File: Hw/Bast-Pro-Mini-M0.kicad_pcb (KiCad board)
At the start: 2 copper layers, 17.8 x 33 mm, 24 parts, among them J1 USB_B_Micro, J2 Conn_02x02_Odd_Even, P1 Digital, P2 ADC, P3 Analog, U1 AP2112K-3.3TRG1, U2 ATSAMD21E18A-AF

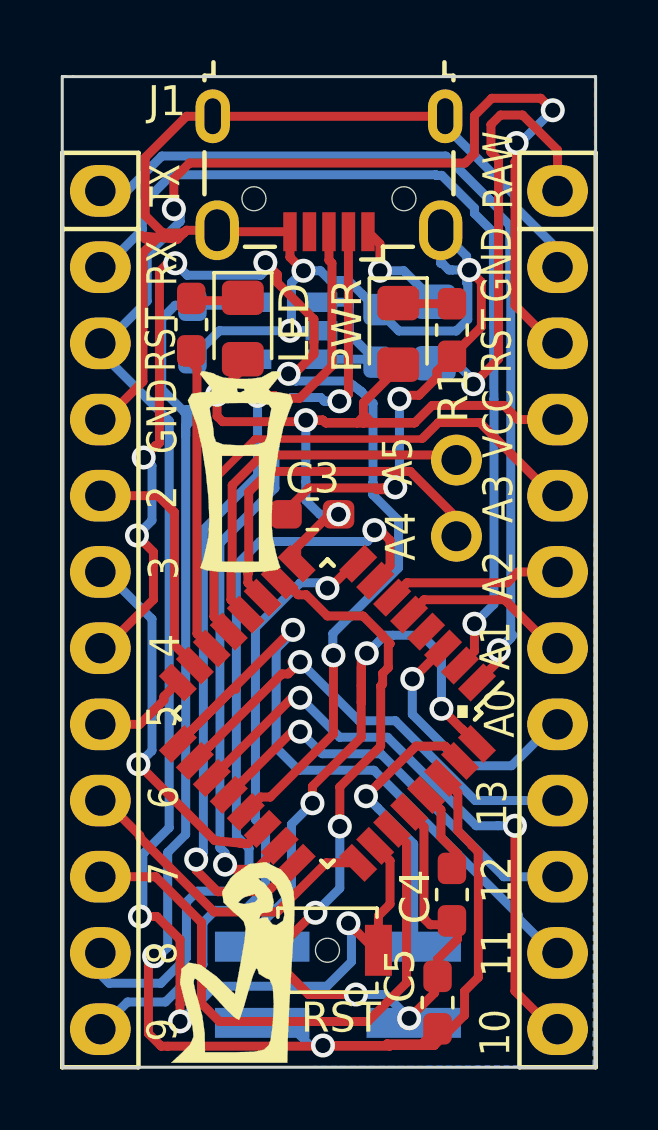
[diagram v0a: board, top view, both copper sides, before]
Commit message: Change type of button
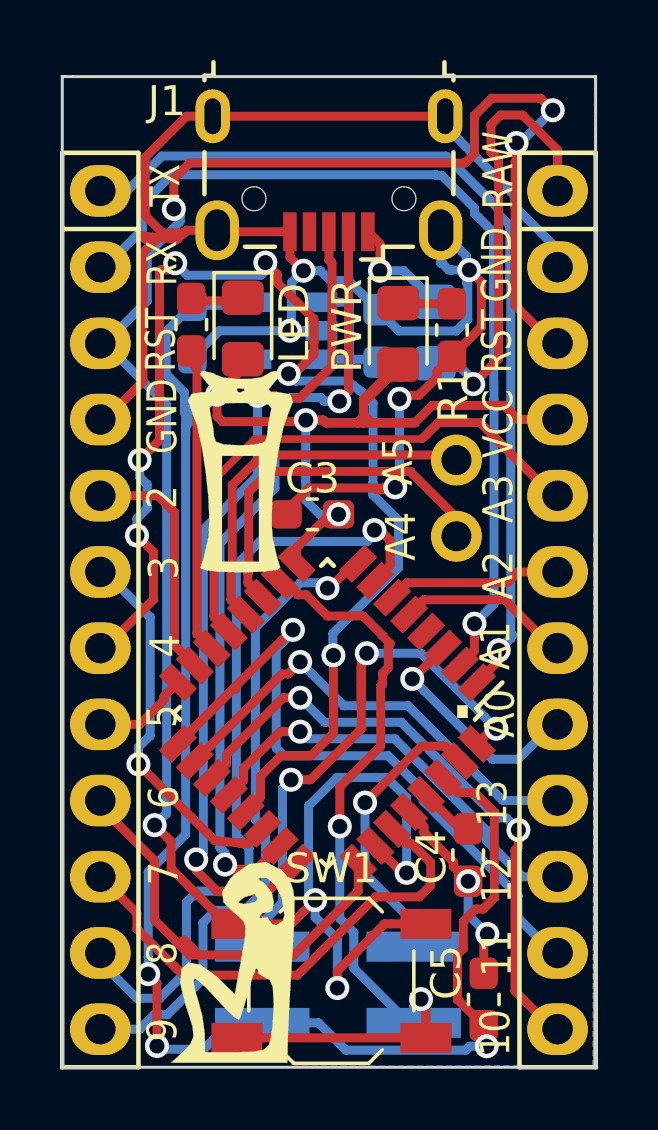
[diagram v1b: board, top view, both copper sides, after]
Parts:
- removed RST: SW_DPST_x2, Button_Switch_SMD:SW_SPST_B3U-1000P-B
- added SW1: SW_DPST_x2, Button_Switch_SMD:SW_SPST_TL3342, F.Cu at (146.1, 111.4)
- moved C5 1.54 mm to (151.2, 112.0)
- moved C4 1.43 mm to (150.7, 107.2)
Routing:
- net /RESET: track 68.9 -> 74.2 mm, vias 6 -> 7
- net +3V3: track 89.3 -> 84.1 mm, vias 5 -> 6
- net GND: track 103.9 -> 107.9 mm
- net /6(**): track 10.9 -> 14.5 mm
- net /7: track 19.6 -> 16.4 mm
- net Net-(C4-Pad1): track 3.01 -> 1.87 mm
- net /A0: track 8.75 -> 7.88 mm
- net /11(**/MOSI): track 24.7 -> 25.2 mm
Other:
- board text added: "v0.3"
- board text removed: "v0.2"
